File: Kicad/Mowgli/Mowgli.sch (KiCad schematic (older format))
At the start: 1 part

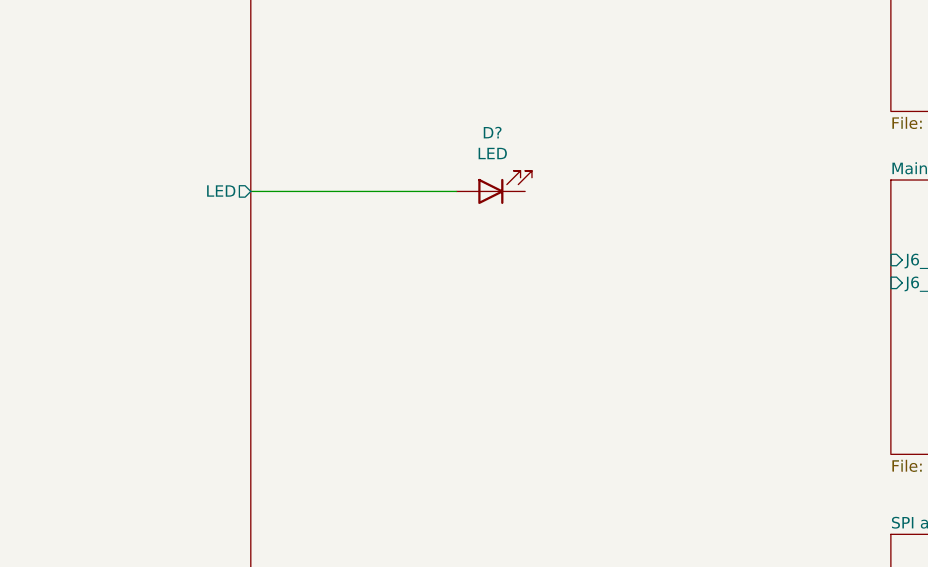
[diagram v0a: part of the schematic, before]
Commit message: added onboard BEEPER
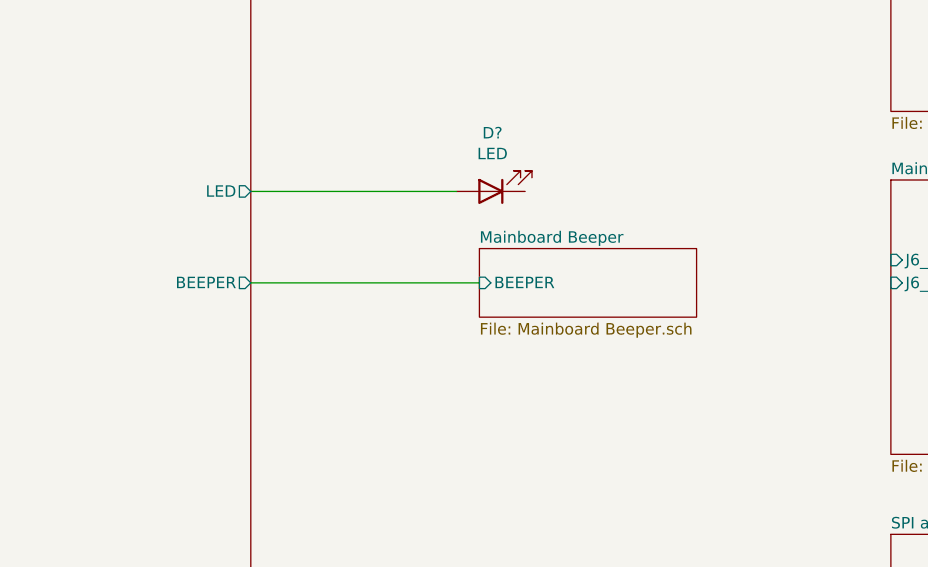
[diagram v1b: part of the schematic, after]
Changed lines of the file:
@@
 $Descr A3 16535 11693
 encoding utf-8
-Sheet 1 13
+Sheet 1 14
 Title "Project Mowgli"
 Date "2022-05-22"
@@
 F34 "BatteryVoltage" I R 9450 2300 59
 F35 "RAIN_Sensor_PE2" I R 9450 5250 50
+F36 "BEEPER" O R 9450 3950 50
 $EndSheet
 Wire Wire Line
@@
 Wire Wire Line
 	4450 8200 5100 8200
-Wire Bus Line
-	6400 7350 6400 7650
-Wire Bus Line
-	7050 6000 7050 6150
-Wire Bus Line
-	9550 5650 9550 5800
-Wire Bus Line
-	12150 5350 12150 5800
-Wire Wire Line
-	3350 5900 5500 5900
-Wire Bus Line
-	7050 950  7050 1650
-Wire Bus Line
-	1550 950  1550 1800
-Wire Bus Line
-	4050 4500 4050 5550
-Wire Bus Line
-	4900 5550 4900 6400
-Wire Bus Line
-	5050 5900 5050 7100
-Wire Bus Line
-	12150 5950 12150 6400
-Wire Bus Line
-	9550 6000 9550 6400
 $Sheet
 S 12250 3500 1600 1200
@@
 F3 "J6_Pin_10_Wheel_blue" I L 12250 3850 50
 $EndSheet
+$Sheet
+S 10450 3800 950  300
+U 62C3C0F1
+F0 "Mainboard Beeper" 50
+F1 "Mainboard Beeper.sch" 50
+F2 "BEEPER" I L 10450 3950 50
+$EndSheet
+Wire Wire Line
+	9450 3950 10450 3950
+Wire Bus Line
+	6400 7350 6400 7650
+Wire Bus Line
+	7050 6000 7050 6150
+Wire Bus Line
+	9550 5650 9550 5800
+Wire Bus Line
+	12150 5350 12150 5800
+Wire Wire Line
+	3350 5900 5500 5900
+Wire Bus Line
+	7050 950  7050 1650
+Wire Bus Line
+	1550 950  1550 1800
+Wire Bus Line
+	4050 4500 4050 5550
+Wire Bus Line
+	4900 5550 4900 6400
+Wire Bus Line
+	5050 5900 5050 7100
+Wire Bus Line
+	12150 5950 12150 6400
+Wire Bus Line
+	9550 6000 9550 6400
 $EndSCHEMATC

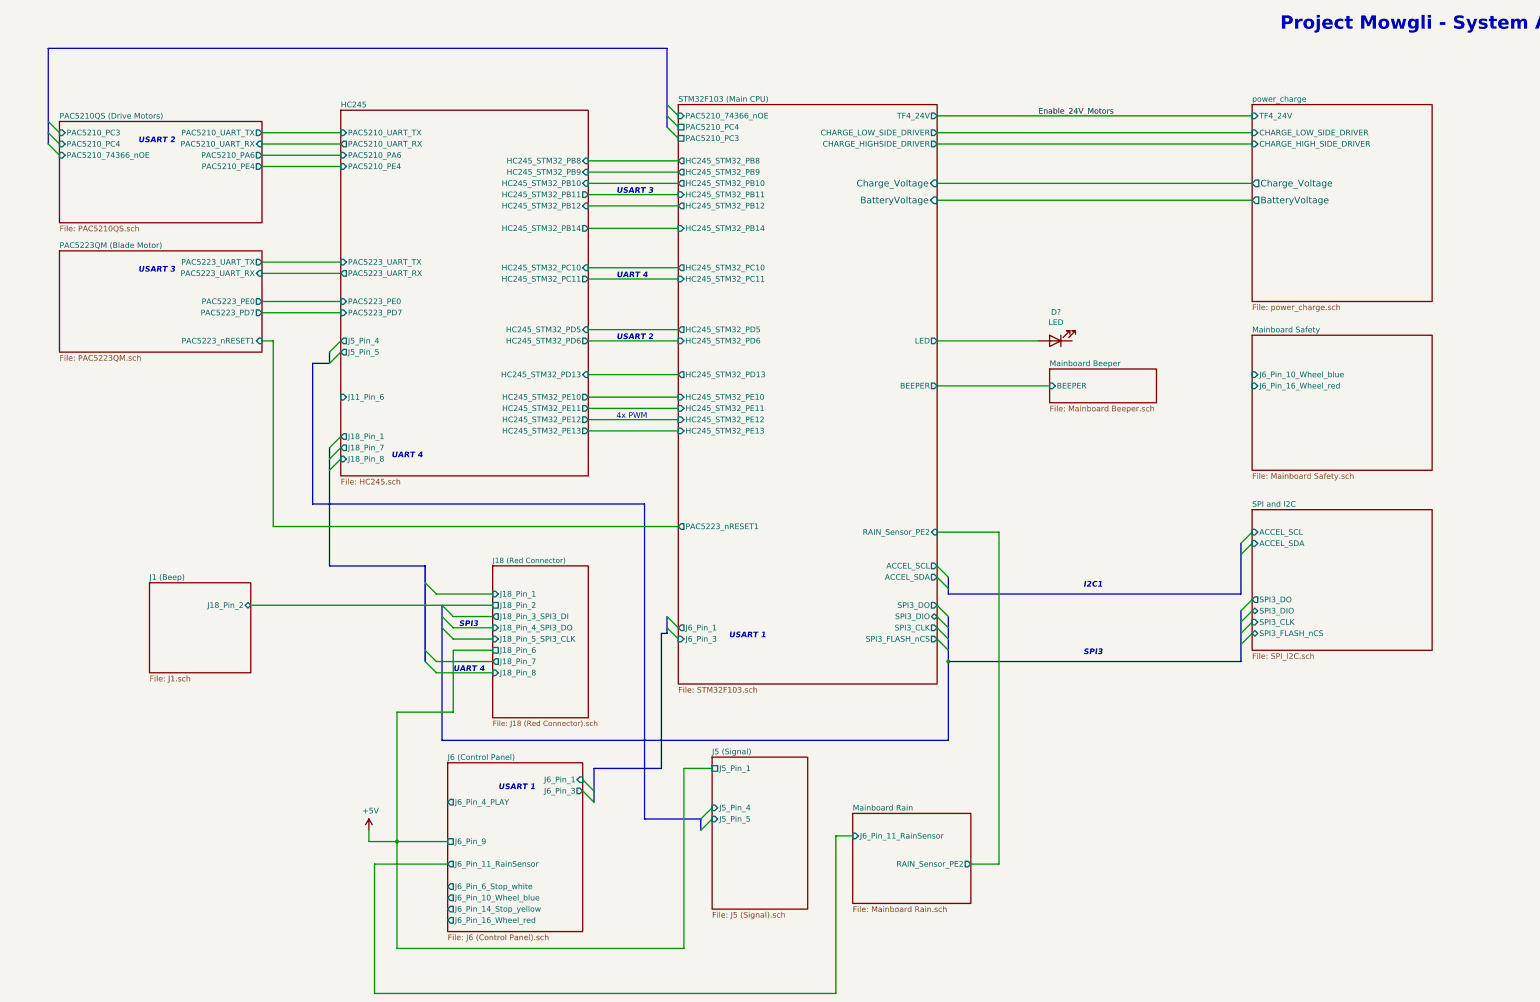
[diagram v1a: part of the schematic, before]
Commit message: reversed mechanical tilt and accelerometer circuit
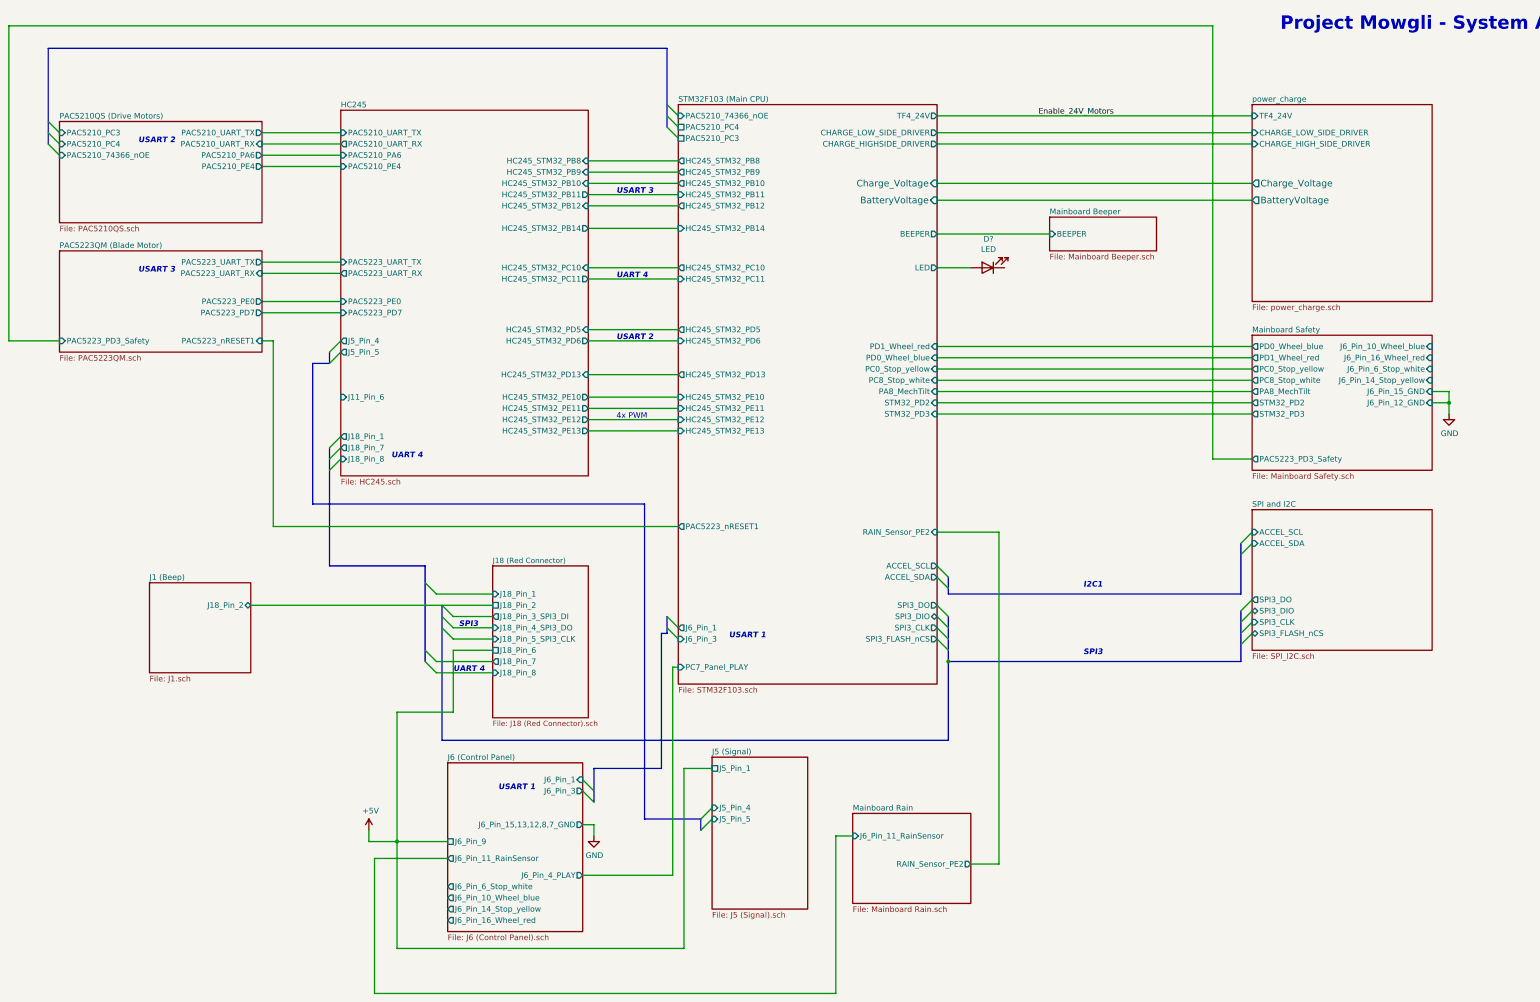
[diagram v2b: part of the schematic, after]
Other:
- moved on the sheet: D?
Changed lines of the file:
@@
 F5 "PAC5223_PE0" O R 3450 3200 50
 F6 "PAC5223_PD7" O R 3450 3300 50
+F7 "PAC5223_PD3_Safety" I L 1650 3550 50
 $EndSheet
 Wire Wire Line
@@
 Wire Wire Line
 	3450 2950 4150 2950
-$Sheet
-S 7150 1450 2300 5150
-U 628D8F35
-F0 "STM32F103 (Main CPU)" 50
-F1 "STM32F103.sch" 50
-F2 "PAC5223_nRESET1" O L 7150 5200 50
-F3 "PAC5210_PC4" U L 7150 1650 50
-F4 "PAC5210_74366_nOE" I L 7150 1550 50
-F5 "PAC5210_PC3" U L 7150 1750 50
-F6 "TF4_24V" O R 9450 1550 50
-F7 "LED" O R 9450 3550 50
-F8 "HC245_STM32_PE10" I L 7150 4050 50
-F9 "HC245_STM32_PE12" I L 7150 4250 50
-F10 "HC245_STM32_PE13" I L 7150 4350 50
-F11 "HC245_STM32_PE11" I L 7150 4150 50
-F12 "HC245_STM32_PB14" I L 7150 2550 50
-F13 "HC245_STM32_PD13" O L 7150 3850 50
-F14 "HC245_STM32_PB8" O L 7150 1950 50
-F15 "HC245_STM32_PB9" O L 7150 2050 50
-F16 "HC245_STM32_PB12" O L 7150 2350 50
-F17 "HC245_STM32_PD5" O L 7150 3450 50
-F18 "HC245_STM32_PD6" I L 7150 3550 50
-F19 "HC245_STM32_PB10" O L 7150 2150 50
-F20 "HC245_STM32_PB11" I L 7150 2250 50
-F21 "HC245_STM32_PC10" O L 7150 2900 50
-F22 "HC245_STM32_PC11" I L 7150 3000 50
-F23 "J6_Pin_1" O L 7150 6100 50
-F24 "J6_Pin_3" I L 7150 6200 50
-F25 "SPI3_DIO" B R 9450 6000 50
-F26 "SPI3_CLK" O R 9450 6100 50
-F27 "SPI3_FLASH_nCS" O R 9450 6200 50
-F28 "SPI3_DO" O R 9450 5900 50
-F29 "ACCEL_SCL" O R 9450 5550 50
-F30 "ACCEL_SDA" O R 9450 5650 50
-F31 "CHARGE_LOW_SIDE_DRIVER" O R 9450 1700 50
-F32 "CHARGE_HIGHSIDE_DRIVER" O R 9450 1800 50
-F33 "Charge_Voltage" I R 9450 2150 59
-F34 "BatteryVoltage" I R 9450 2300 59
-F35 "RAIN_Sensor_PE2" I R 9450 5250 50
-F36 "BEEPER" O R 9450 3950 50
-$EndSheet
 Wire Wire Line
 	3450 3550 3550 3550
@@
 L Device:LED D?
 U 1 1 628F5BF0
-P 10500 3550
-F 0 "D?" H 10493 3295 50  0000 C CNN
-F 1 "LED" H 10493 3386 50  0000 C CNN
-F 2 "" H 10500 3550 50  0001 C CNN
-F 3 "~" H 10500 3550 50  0001 C CNN
-	1    10500 3550
+P 9900 2900
+F 0 "D?" H 9893 2645 50  0000 C CNN
+F 1 "LED" H 9893 2736 50  0000 C CNN
+F 2 "" H 9900 2900 50  0001 C CNN
+F 3 "~" H 9900 2900 50  0001 C CNN
+	1    9900 2900
 	-1   0    0    1
 $EndComp
-Wire Wire Line
-	10350 3550 9450 3550
 Entry Wire Line
 	7050 1650 7150 1750
@@
 F7 "J6_Pin_6_Stop_white" O L 5100 8400 50
 F8 "J6_Pin_16_Wheel_red" O L 5100 8700 50
-F9 "J6_Pin_4_PLAY" O L 5100 7650 50
-F10 "J6_Pin_11_RainSensor" O L 5100 8200 50
+F9 "J6_Pin_4_PLAY" O R 6300 8300 50
+F10 "J6_Pin_11_RainSensor" O L 5100 8150 50
+F11 "J6_Pin_15,13,12,8,7_GND" O R 6300 7850 50
 $EndSheet
 $Sheet
@@
 Wire Wire Line
 	8550 9350 4450 9350
-Wire Wire Line
-	4450 9350 4450 8200
-Wire Wire Line
-	4450 8200 5100 8200
 $Sheet
 S 12250 3500 1600 1200
@@
 F0 "Mainboard Safety" 50
 F1 "Mainboard Safety.sch" 50
-F2 "J6_Pin_16_Wheel_red" I L 12250 3950 50
-F3 "J6_Pin_10_Wheel_blue" I L 12250 3850 50
-$EndSheet
-$Sheet
-S 10450 3800 950  300
+F2 "J6_Pin_16_Wheel_red" I R 13850 3700 50
+F3 "J6_Pin_10_Wheel_blue" I R 13850 3600 50
+F4 "PD1_Wheel_red" O L 12250 3700 50
+F5 "PD0_Wheel_blue" O L 12250 3600 50
+F6 "J6_Pin_6_Stop_white" I R 13850 3800 50
+F7 "J6_Pin_14_Stop_yellow" I R 13850 3900 50
+F8 "PC0_Stop_yellow" O L 12250 3800 50
+F9 "STM32_PD2" O L 12250 4100 50
+F10 "PC8_Stop_white" O L 12250 3900 50
+F11 "STM32_PD3" O L 12250 4200 50
+F12 "J6_Pin_15_GND" I R 13850 4000 50
+F13 "J6_Pin_12_GND" I R 13850 4100 50
+F14 "PA8_MechTilt" O L 12250 4000 50
+F15 "PAC5223_PD3_Safety" O L 12250 4600 50
+$EndSheet
+$Sheet
+S 10450 2450 950  300
 U 62C3C0F1
 F0 "Mainboard Beeper" 50
 F1 "Mainboard Beeper.sch" 50
-F2 "BEEPER" I L 10450 3950 50
-$EndSheet
-Wire Wire Line
-	9450 3950 10450 3950
+F2 "BEEPER" I L 10450 2600 50
+$EndSheet
+Wire Wire Line
+	9450 2600 10450 2600
+Wire Wire Line
+	9750 2900 9450 2900
+Wire Wire Line
+	12250 3900 9450 3900
+Wire Wire Line
+	12250 3800 9450 3800
+Wire Wire Line
+	9450 3700 12250 3700
+Wire Wire Line
+	12250 3600 9450 3600
+$Comp
+L power:GND #PWR?
+U 1 1 62B0D03C
+P 14000 4200
+F 0 "#PWR?" H 14000 3950 50  0001 C CNN
+F 1 "GND" H 14005 4027 50  0000 C CNN
+F 2 "" H 14000 4200 50  0001 C CNN
+F 3 "" H 14000 4200 50  0001 C CNN
+	1    14000 4200
+	1    0    0    -1
+$EndComp
+Wire Wire Line
+	13850 4000 14000 4000
+Wire Wire Line
+	14000 4000 14000 4100
+$Comp
+L power:GND #PWR?
+U 1 1 62B0FECA
+P 6400 7950
+F 0 "#PWR?" H 6400 7700 50  0001 C CNN
+F 1 "GND" H 6405 7777 50  0000 C CNN
+F 2 "" H 6400 7950 50  0001 C CNN
+F 3 "" H 6400 7950 50  0001 C CNN
+	1    6400 7950
+	1    0    0    -1
+$EndComp
+Wire Wire Line
+	6300 7850 6400 7850
+Wire Wire Line
+	6400 7850 6400 7950
+Wire Wire Line
+	13850 4100 14000 4100
+Wire Wire Line
+	14000 4200 14000 4100
+Connection ~ 14000 4100
+Wire Wire Line
+	12250 4000 9450 4000
+Wire Wire Line
+	12250 4600 11900 4600
+Wire Wire Line
+	11900 4600 11900 750
+Wire Wire Line
+	11900 750  1200 750
+Wire Wire Line
+	1200 750  1200 3550
+Wire Wire Line
+	1200 3550 1650 3550
+$Sheet
+S 7150 1450 2300 5150
+U 628D8F35
+F0 "STM32F103 (Main CPU)" 50
+F1 "STM32F103.sch" 50
+F2 "PAC5223_nRESET1" O L 7150 5200 50
+F3 "PAC5210_PC4" U L 7150 1650 50
+F4 "PAC5210_74366_nOE" I L 7150 1550 50
+F5 "PAC5210_PC3" U L 7150 1750 50
+F6 "TF4_24V" O R 9450 1550 50
+F7 "LED" O R 9450 2900 50
+F8 "HC245_STM32_PE10" I L 7150 4050 50
+F9 "HC245_STM32_PE12" I L 7150 4250 50
+F10 "HC245_STM32_PE13" I L 7150 4350 50
+F11 "HC245_STM32_PE11" I L 7150 4150 50
+F12 "HC245_STM32_PB14" I L 7150 2550 50
+F13 "HC245_STM32_PD13" O L 7150 3850 50
+F14 "HC245_STM32_PB8" O L 7150 1950 50
+F15 "HC245_STM32_PB9" O L 7150 2050 50
+F16 "HC245_STM32_PB12" O L 7150 2350 50
+F17 "HC245_STM32_PD5" O L 7150 3450 50
+F18 "HC245_STM32_PD6" I L 7150 3550 50
+F19 "HC245_STM32_PB10" O L 7150 2150 50
+F20 "HC245_STM32_PB11" I L 7150 2250 50
+F21 "HC245_STM32_PC10" O L 7150 2900 50
+F22 "HC245_STM32_PC11" I L 7150 3000 50
+F23 "J6_Pin_1" O L 7150 6100 50
+F24 "J6_Pin_3" I L 7150 6200 50
+F25 "SPI3_DIO" B R 9450 6000 50
+F26 "SPI3_CLK" O R 9450 6100 50
+F27 "SPI3_FLASH_nCS" O R 9450 6200 50
+F28 "SPI3_DO" O R 9450 5900 50
+F29 "ACCEL_SCL" O R 9450 5550 50
+F30 "ACCEL_SDA" O R 9450 5650 50
+F31 "CHARGE_LOW_SIDE_DRIVER" O R 9450 1700 50
+F32 "CHARGE_HIGHSIDE_DRIVER" O R 9450 1800 50
+F33 "Charge_Voltage" I R 9450 2150 59
+F34 "BatteryVoltage" I R 9450 2300 59
+F35 "RAIN_Sensor_PE2" I R 9450 5250 50
+F36 "BEEPER" O R 9450 2600 50
+F37 "PD1_Wheel_red" I R 9450 3600 50
+F38 "PD0_Wheel_blue" I R 9450 3700 50
+F39 "PC0_Stop_yellow" I R 9450 3800 50
+F40 "PC8_Stop_white" I R 9450 3900 50
+F41 "PA8_MechTilt" I R 9450 4000 50
+F42 "STM32_PD2" I R 9450 4100 50
+F43 "STM32_PD3" I R 9450 4200 50
+F44 "PC7_Panel_PLAY" I L 7150 6450 50
+$EndSheet
+Wire Wire Line
+	12250 4100 9450 4100
+Wire Wire Line
+	12250 4200 9450 4200
+Wire Wire Line
+	7150 6450 7100 6450
+Wire Wire Line
+	7100 6450 7100 8300
+Wire Wire Line
+	7100 8300 6300 8300
+Wire Wire Line
+	5100 8150 4450 8150
+Wire Wire Line
+	4450 8150 4450 9350
 Wire Bus Line
 	6400 7350 6400 7650

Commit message: added Panel Eliminator
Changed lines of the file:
@@
 Text Notes 10750 6350 0    50   Italic 10
 SPI3
-Text Notes 12500 800  0    118  ~ 24
+Text Notes 12200 1000 0    118  ~ 24
 Project Mowgli - System Architecture
 $Sheet
